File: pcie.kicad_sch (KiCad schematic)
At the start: 29 parts, among them J8 Bus_M.2_Socket_M, U1 MIMX8MM6DVTLZAA, U17 SI52112-B5-GM2, U24 74LVC1G07, U25 74LVC1G07, Y3 25MHz

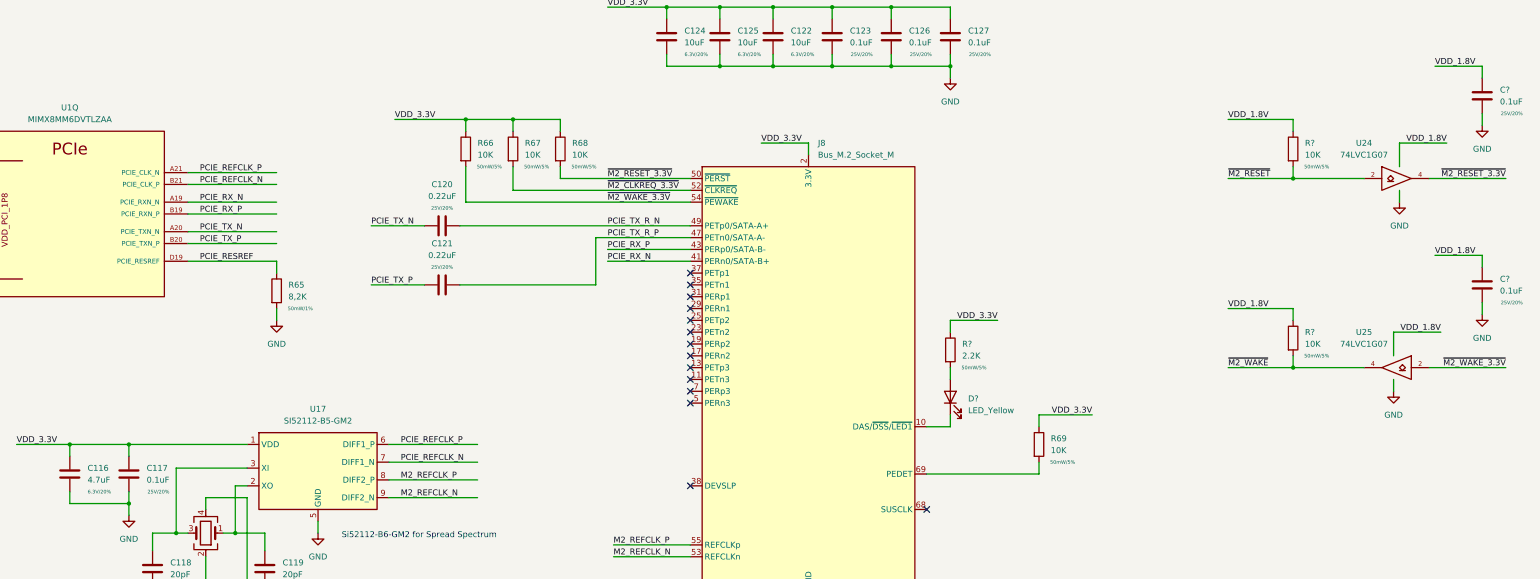
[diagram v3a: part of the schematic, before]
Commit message: ddr: add dual die support, misc work
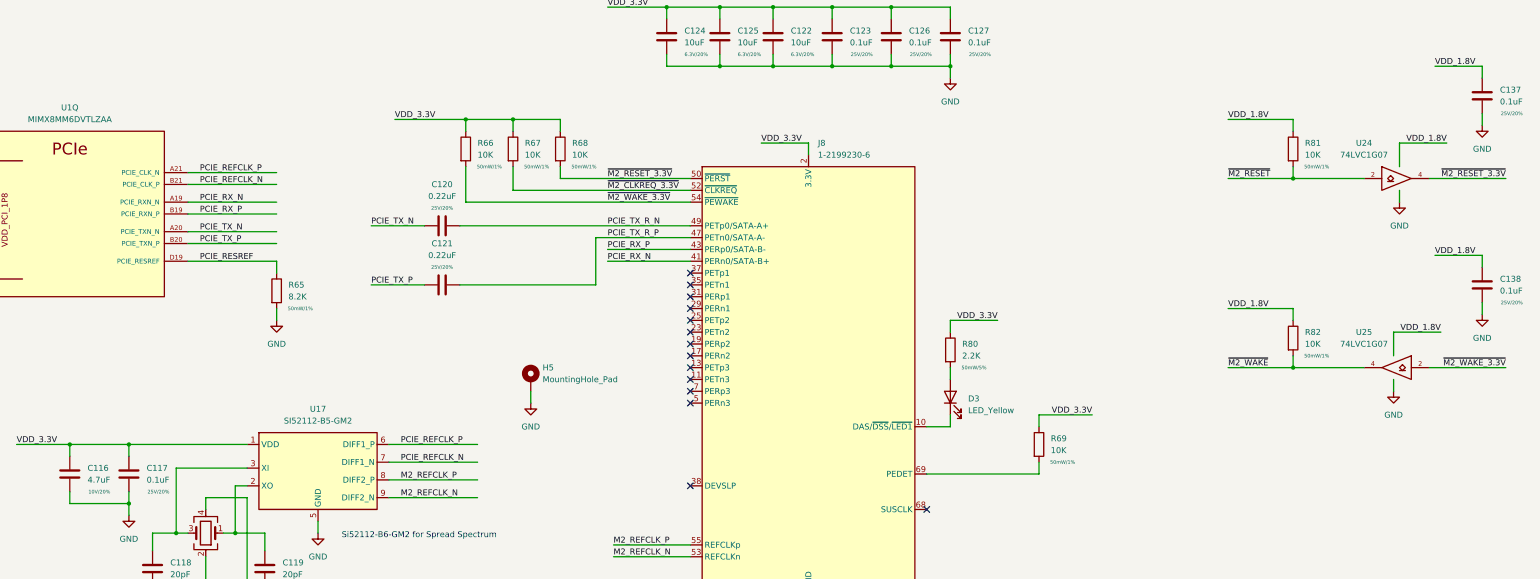
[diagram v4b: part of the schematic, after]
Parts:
- added H5: MountingHole_Pad, Mounting_Wuerth:Mounting_Wuerth_WA-SMSI-M3_H2.5mm_9774025360, symbol Mechanical:MountingHole_Pad
- C116: Rating 6.3V/20% -> 10V/20%
- C122, C124, C125: footprint Capacitor_SMD:C_0603_1608Metric -> Capacitor_SMD:C_0402_1005Metric
- J8: value Bus_M.2_Socket_M -> 1-2199230-6
- R65: value 8,2K -> 8.2K
- R66, R67, R68, R69: Rating 50mW/5% -> 50mW/1%
- R81, R82: renamed from R?; Rating 50mW/5% -> 50mW/1%
- U24, U25: footprint Package_TO_SOT_SMD:SOT-553 -> Package_TO_SOT_SMD:SOT-23-5
- Y3: footprint (none) -> Crystal:Crystal_SMD_3225-4Pin_3.2x2.5mm
- gave numbers to parts that had none: 4
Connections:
- net GND: now also H5.1
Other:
- company: (none) -> Q-LAB
- title: (none) -> QSBC
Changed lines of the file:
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@@
 (kicad_sch (version 20211123) (generator eeschema)
   (paper "A3")
+  (title_block
+    (title "QSBC")
+    (rev "1")
+    (company "Q-LAB")
+  )
   (junction (at 241.3 36.83) (diameter 0) (color 0 0 0 0)
   )
@@
     (stroke (width 0) (type default) (color 0 0 0 0))
   )
+  (wire (pts (xy 176.53 106.68) (xy 176.53 109.22))
+    (stroke (width 0) (type default) (color 0 0 0 0))
+  )
   (wire (pts (xy 285.75 111.76) (xy 285.75 114.3))
     (stroke (width 0) (type default) (color 0 0 0 0))
@@
     (property "Reference" "Y3" (id 0) (at 100.33 156.21 0))
     (property "Value" "25MHz" (id 1) (at 105.41 153.67 0))
-    (property "Footprint" "" (id 2) (at 106.68 137.16 0)
+    (property "Footprint" "Crystal:Crystal_SMD_3225-4Pin_3.2x2.5mm" (id 2) (at 106.68 137.16 0)
       (effects (font (size 1.27 1.27)) hide)
     )
@@
   (symbol (lib_id "power:GND") (at 236.22 154.94 0) (unit 1)
     (in_bom yes) (on_board yes) (fields_autoplaced)
-    (property "Reference" "#PWR?" (id 0) (at 236.22 161.29 0)
+    (property "Reference" "#PWR0230" (id 0) (at 236.22 161.29 0)
       (effects (font (size 1.27 1.27)) hide)
     )
@@
   (symbol (lib_id "Device:C") (at 381 43.18 0) (unit 1)
     (in_bom yes) (on_board yes)
-    (property "Reference" "C?" (id 0) (at 384.81 41.9099 0)
+    (property "Reference" "C137" (id 0) (at 384.81 41.9099 0)
       (effects (font (size 1.27 1.27)) (justify left))
     )
@@
     (property "Reference" "U25" (id 0) (at 355.6 93.98 0))
     (property "Value" "74LVC1G07" (id 1) (at 355.6 96.52 0))
-    (property "Footprint" "Package_TO_SOT_SMD:SOT-553" (id 2) (at 361.95 101.6 0)
+    (property "Footprint" "Package_TO_SOT_SMD:SOT-23-5" (id 2) (at 361.95 101.6 0)
       (effects (font (size 1.27 1.27)) hide)
     )
@@
   (symbol (lib_id "Device:R") (at 266.7 97.79 0) (unit 1)
     (in_bom yes) (on_board yes)
-    (property "Reference" "R?" (id 0) (at 269.24 96.5199 0)
+    (property "Reference" "R80" (id 0) (at 269.24 96.5199 0)
       (effects (font (size 1.27 1.27)) (justify left))
     )
@@
     (property "Reference" "U24" (id 0) (at 355.6 53.34 0))
     (property "Value" "74LVC1G07" (id 1) (at 355.6 55.88 0))
-    (property "Footprint" "Package_TO_SOT_SMD:SOT-553" (id 2) (at 363.22 60.96 0)
+    (property "Footprint" "Package_TO_SOT_SMD:SOT-23-5" (id 2) (at 363.22 60.96 0)
       (effects (font (size 1.27 1.27)) hide)
     )
@@
       (effects (font (size 1.27 1.27)) (justify left))
     )
-    (property "Footprint" "Capacitor_SMD:C_0603_1608Metric" (id 2) (at 229.5652 34.29 0)
+    (property "Footprint" "Capacitor_SMD:C_0402_1005Metric" (id 2) (at 229.5652 34.29 0)
       (effects (font (size 1.27 1.27)) hide)
     )
@@
       (effects (font (size 1.27 1.27)) (justify left))
     )
-    (property "Value" "8,2K" (id 1) (at 124.46 86.3599 0)
+    (property "Value" "8.2K" (id 1) (at 124.46 86.3599 0)
       (effects (font (size 1.27 1.27)) (justify left))
     )
@@
     (pin "2")
   )
+  (symbol (lib_id "Mechanical:MountingHole_Pad") (at 176.53 104.14 0) (unit 1)
+    (in_bom yes) (on_board yes) (fields_autoplaced)
+    (property "Reference" "H5" (id 0) (at 179.07 101.5999 0)
+      (effects (font (size 1.27 1.27)) (justify left))
+    )
+    (property "Value" "MountingHole_Pad" (id 1) (at 179.07 104.1399 0)
+      (effects (font (size 1.27 1.27)) (justify left))
+    )
+    (property "Footprint" "Mounting_Wuerth:Mounting_Wuerth_WA-SMSI-M3_H2.5mm_9774025360" (id 2) (at 176.53 104.14 0)
+      (effects (font (size 1.27 1.27)) hide)
+    )
+    (property "Datasheet" "~" (id 3) (at 176.53 104.14 0)
+      (effects (font (size 1.27 1.27)) hide)
+    )
+    (pin "1")
+  )
   (symbol (lib_id "Device:C") (at 241.3 30.48 0) (unit 1)
     (in_bom yes) (on_board yes)
@@
   (symbol (lib_id "Device:R") (at 340.36 54.61 0) (unit 1)
     (in_bom yes) (on_board yes)
-    (property "Reference" "R?" (id 0) (at 342.9 53.3399 0)
+    (property "Reference" "R81" (id 0) (at 342.9 53.3399 0)
       (effects (font (size 1.27 1.27)) (justify left))
     )
@@
       (effects (font (size 1.27 1.27)) hide)
     )
-    (property "Rating" "50mW/5%" (id 4) (at 345.44 58.42 0)
+    (property "Rating" "50mW/1%" (id 4) (at 345.44 58.42 0)
       (effects (font (size 0.762 0.762)))
     )
@@
       (effects (font (size 1.27 1.27)) hide)
     )
-    (property "Rating" "50mW/5%" (id 4) (at 177.8 58.42 0)
+    (property "Rating" "50mW/1%" (id 4) (at 177.8 58.42 0)
       (effects (font (size 0.762 0.762)))
     )
@@
       (effects (font (size 1.27 1.27)) hide)
     )
-    (property "Rating" "50mW/5%" (id 4) (at 290.83 121.92 0)
+    (property "Rating" "50mW/1%" (id 4) (at 290.83 121.92 0)
       (effects (font (size 0.762 0.762)))
     )
@@
       (effects (font (size 1.27 1.27)) hide)
     )
-    (property "Rating" "50mW/5%" (id 4) (at 187.96 58.42 0)
+    (property "Rating" "50mW/1%" (id 4) (at 187.96 58.42 0)
       (effects (font (size 0.762 0.762)))
     )
@@
   (symbol (lib_id "power:GND") (at 361.95 106.68 0) (unit 1)
     (in_bom yes) (on_board yes) (fields_autoplaced)
-    (property "Reference" "#PWR?" (id 0) (at 361.95 113.03 0)
+    (property "Reference" "#PWR0228" (id 0) (at 361.95 113.03 0)
       (effects (font (size 1.27 1.27)) hide)
     )
@@
   (symbol (lib_id "power:GND") (at 363.22 66.04 0) (unit 1)
     (in_bom yes) (on_board yes) (fields_autoplaced)
-    (property "Reference" "#PWR?" (id 0) (at 363.22 72.39 0)
+    (property "Reference" "#PWR0226" (id 0) (at 363.22 72.39 0)
       (effects (font (size 1.27 1.27)) hide)
     )
@@
   (symbol (lib_id "Device:C") (at 381 83.82 0) (unit 1)
     (in_bom yes) (on_board yes)
-    (property "Reference" "C?" (id 0) (at 384.81 82.5499 0)
+    (property "Reference" "C138" (id 0) (at 384.81 82.5499 0)
       (effects (font (size 1.27 1.27)) (justify left))
     )
@@
       (effects (font (size 1.27 1.27)) hide)
     )
-    (property "Rating" "6.3V/20%" (id 4) (at 83.82 128.27 0)
+    (property "Rating" "10V/20%" (id 4) (at 83.82 128.27 0)
       (effects (font (size 0.762 0.762)))
     )
@@
   (symbol (lib_id "power:GND") (at 381 49.53 0) (unit 1)
     (in_bom yes) (on_board yes) (fields_autoplaced)
-    (property "Reference" "#PWR?" (id 0) (at 381 55.88 0)
+    (property "Reference" "#PWR0227" (id 0) (at 381 55.88 0)
       (effects (font (size 1.27 1.27)) hide)
     )
@@
       (effects (font (size 1.27 1.27)) hide)
     )
-    (property "Rating" "50mW/5%" (id 4) (at 167.64 58.42 0)
+    (property "Rating" "50mW/1%" (id 4) (at 167.64 58.42 0)
       (effects (font (size 0.762 0.762)))
     )
@@
   (symbol (lib_id "Device:LED") (at 266.7 107.95 90) (unit 1)
     (in_bom yes) (on_board yes) (fields_autoplaced)
-    (property "Reference" "D?" (id 0) (at 270.51 108.2674 90)
+    (property "Reference" "D3" (id 0) (at 270.51 108.2674 90)
       (effects (font (size 1.27 1.27)) (justify right))
     )
@@
   (symbol (lib_id "power:GND") (at 381 90.17 0) (unit 1)
     (in_bom yes) (on_board yes) (fields_autoplaced)
-    (property "Reference" "#PWR?" (id 0) (at 381 96.52 0)
+    (property "Reference" "#PWR0229" (id 0) (at 381 96.52 0)
       (effects (font (size 1.27 1.27)) hide)
     )
@@
       (effects (font (size 1.27 1.27)) (justify left))
     )
-    (property "Value" "Bus_M.2_Socket_M" (id 1) (at 238.2394 55.88 0)
+    (property "Value" "1-2199230-6" (id 1) (at 238.2394 55.88 0)
       (effects (font (size 1.27 1.27)) (justify left))
     )
@@
       (effects (font (size 1.27 1.27)) (justify left))
     )
-    (property "Footprint" "Capacitor_SMD:C_0603_1608Metric" (id 2) (at 218.1352 34.29 0)
+    (property "Footprint" "Capacitor_SMD:C_0402_1005Metric" (id 2) (at 218.1352 34.29 0)
       (effects (font (size 1.27 1.27)) hide)
     )
@@
       (effects (font (size 1.27 1.27)) (justify left))
     )
-    (property "Footprint" "Capacitor_SMD:C_0603_1608Metric" (id 2) (at 206.7052 34.29 0)
+    (property "Footprint" "Capacitor_SMD:C_0402_1005Metric" (id 2) (at 206.7052 34.29 0)
       (effects (font (size 1.27 1.27)) hide)
     )
@@
     (pin "2")
   )
+  (symbol (lib_id "power:GND") (at 176.53 109.22 0) (unit 1)
+    (in_bom yes) (on_board yes) (fields_autoplaced)
+    (property "Reference" "#PWR0235" (id 0) (at 176.53 115.57 0)
+      (effects (font (size 1.27 1.27)) hide)
+    )
+    (property "Value" "GND" (id 1) (at 176.53 114.3 0))
+    (property "Footprint" "" (id 2) (at 176.53 109.22 0)
+      (effects (font (size 1.27 1.27)) hide)
+    )
+    (property "Datasheet" "" (id 3) (at 176.53 109.22 0)
+      (effects (font (size 1.27 1.27)) hide)
+    )
+    (pin "1")
+  )
   (symbol (lib_id "Device:R") (at 340.36 95.25 0) (unit 1)
     (in_bom yes) (on_board yes)
-    (property "Reference" "R?" (id 0) (at 342.9 93.9799 0)
+    (property "Reference" "R82" (id 0) (at 342.9 93.9799 0)
       (effects (font (size 1.27 1.27)) (justify left))
     )
@@
       (effects (font (size 1.27 1.27)) hide)
     )
-    (property "Rating" "50mW/5%" (id 4) (at 345.44 99.06 0)
-      (effects (font (size 0.762 0.762)))
-    )
+    (property "Rating" "50mW/1%" (id 4) (at 345.44 99.06 0)
+      (effects (font (size 0.762 0.762)))
+    )

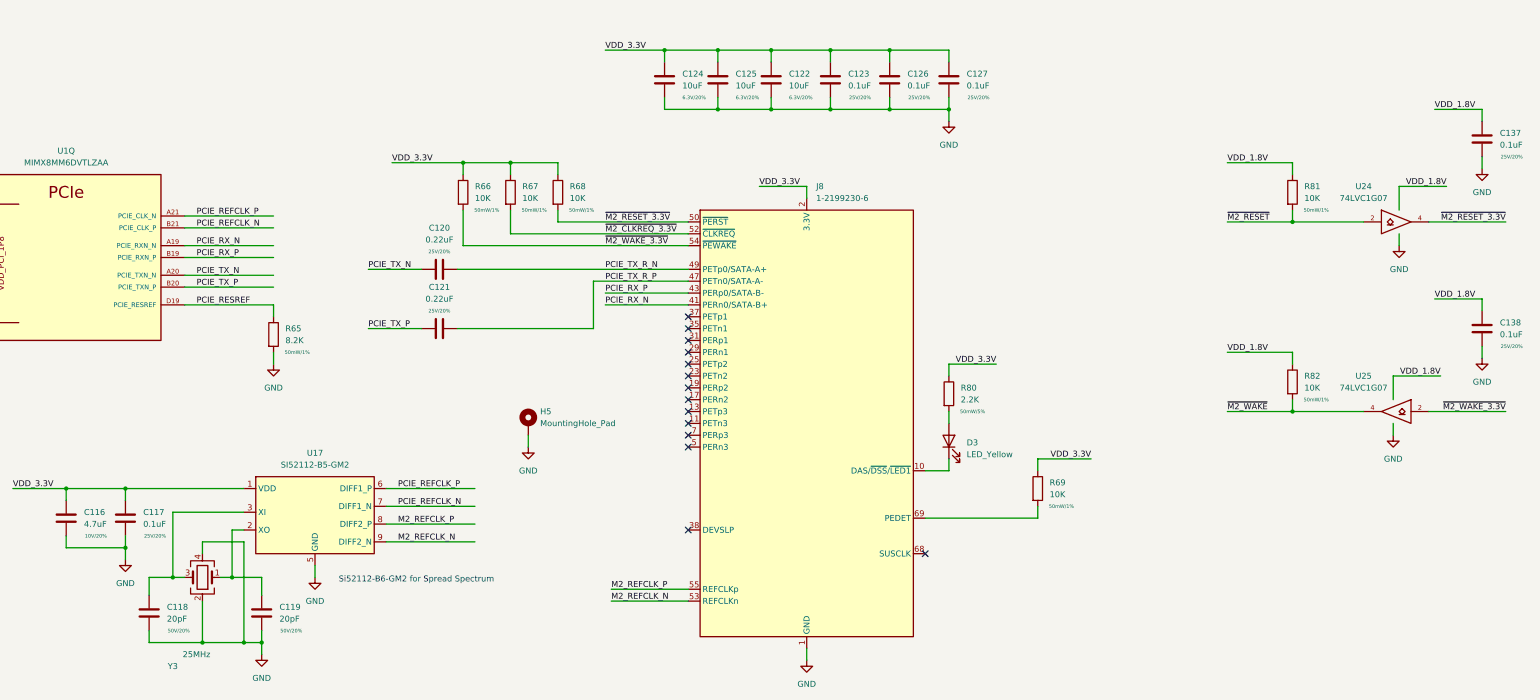
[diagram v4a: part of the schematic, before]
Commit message: fix ref desgigators, add table for dram config
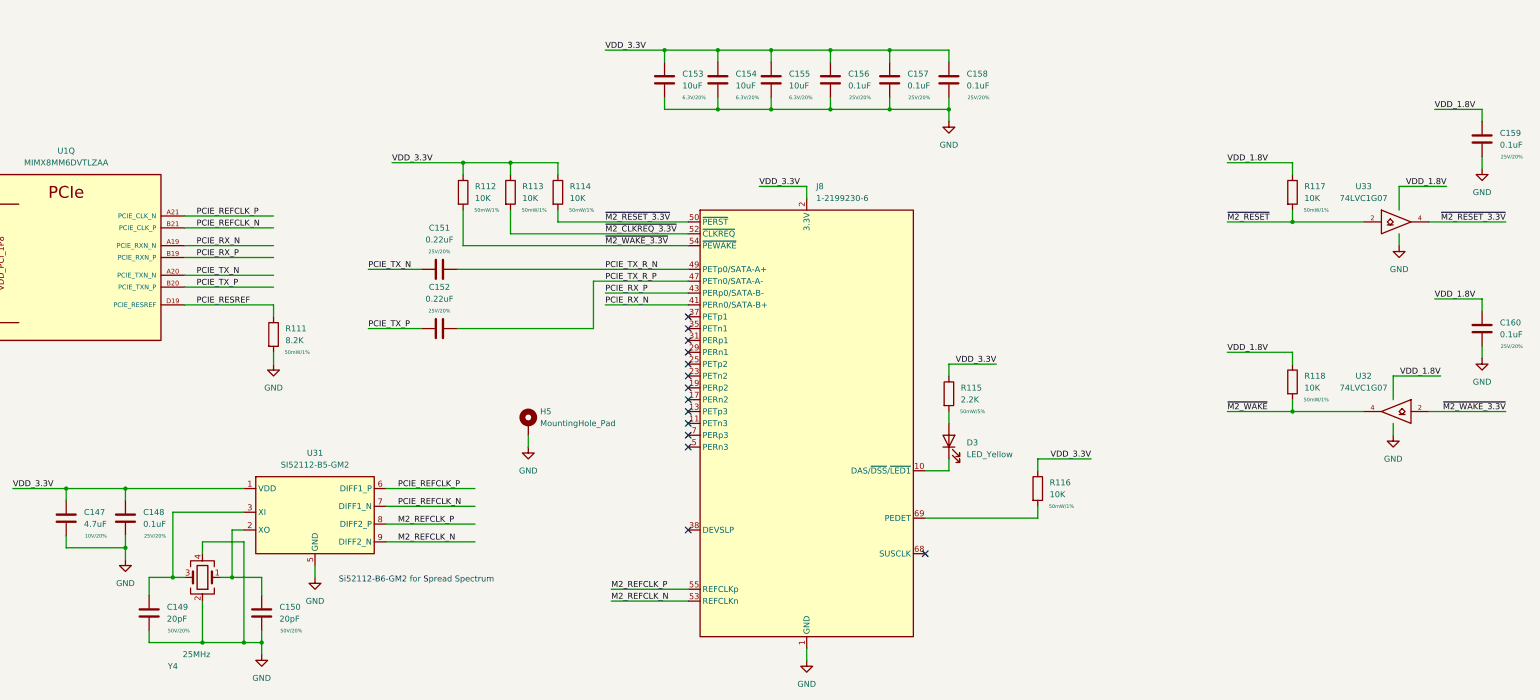
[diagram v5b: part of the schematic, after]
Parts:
- renumbered C116 to C147, C117 to C148, C118 to C149, C119 to C150, C120 to C151, C121 to C152, C124 to C153, C125 to C154, C122 to C155, C123 to C156, C126 to C157, C127 to C158, C137 to C159, C138 to C160, R65 to R111, R66 to R112, R67 to R113, R68 to R114, R80 to R115, R69 to R116, R81 to R117, R82 to R118, U17 to U31, U25 to U32, U24 to U33, Y3 to Y4

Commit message: add inital ddr tool version, lots of routing work
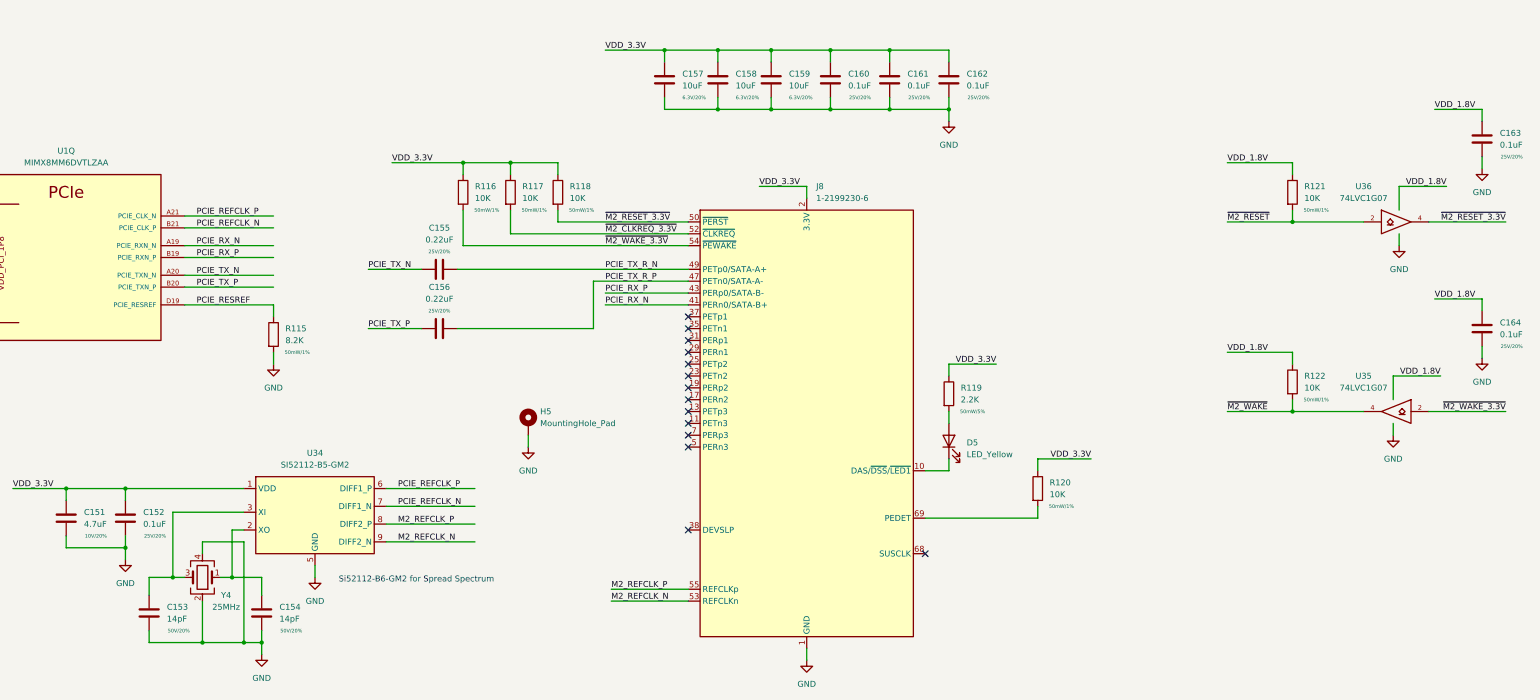
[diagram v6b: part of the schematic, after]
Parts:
- C153: renamed from C149; value 20pF -> 14pF
- C154: renamed from C150; value 20pF -> 14pF
- Y4: MPN (none) -> ECS-250-10-33B-CWN-TR
- renumbered C147 to C151, C148 to C152, C151 to C155, C152 to C156, C153 to C157, C154 to C158, C155 to C159, C156 to C160, C157 to C161, C158 to C162, C159 to C163, C160 to C164, D3 to D5, R111 to R115, R112 to R116, R113 to R117, R114 to R118, R115 to R119, R116 to R120, R117 to R121, R118 to R122, U31 to U34, U32 to U35, U33 to U36
